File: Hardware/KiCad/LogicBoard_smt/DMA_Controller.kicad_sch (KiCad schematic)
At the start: 49 parts, among them IC1 7408N, IC18 7432N, IC20 7430N, IC21 7400N, IC3 74573N, IC31 7400N, IC32 7432N, IC5 7400N, IC53 7404N, IC9 7474N, U3 GFXL, U4 GFXH, U5 GFYL, U6 GFYH, U7 74LVC2G07

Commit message: updates to kicad smt versions
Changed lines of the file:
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@@
     (stroke (width 0.1524) (type solid))
   )
-  (wire (pts (xy 515.62 901.7) (xy 515.62 891.54))
+  (wire (pts (xy 515.62 901.7) (xy 515.62 892.81))
     (stroke (width 0.1524) (type solid))
   )
@@
     (stroke (width 0) (type default))
   )
-  (wire (pts (xy 520.7 901.7) (xy 515.62 901.7))
+  (wire (pts (xy 515.62 901.7) (xy 520.7 901.7))
     (stroke (width 0.1524) (type solid))
   )
@@
     (stroke (width 0.1524) (type solid))
   )
-  (wire (pts (xy 515.62 891.54) (xy 546.1 891.54))
+  (wire (pts (xy 515.62 892.81) (xy 546.1 892.81))
     (stroke (width 0.1524) (type solid))
   )
@@
     (stroke (width 0.1524) (type solid))
   )
-  (wire (pts (xy 513.08 741.68) (xy 513.08 474.98))
+  (wire (pts (xy 513.08 474.98) (xy 513.08 741.68))
     (stroke (width 0.1524) (type solid))
   )
@@
     (stroke (width 0) (type default))
   )
-  (wire (pts (xy 546.1 891.54) (xy 546.1 868.68))
+  (wire (pts (xy 546.1 892.81) (xy 546.1 868.68))
     (stroke (width 0.1524) (type solid))
   )
@@
     (stroke (width 0.1524) (type solid))
   )
+  (wire (pts (xy 513.08 711.2) (xy 513.08 708.66))
+    (stroke (width 0) (type default))
+  )
   (wire (pts (xy 462.28 1122.68) (xy 464.82 1122.68))
     (stroke (width 0.1524) (type solid))
@@
     (effects (font (size 1.27 1.27)) (justify left bottom))
   )
-  (label "~{INIT}" (at 513.08 708.66 90) (fields_autoplaced)
+  (label "~{INIT}" (at 513.08 711.2 90) (fields_autoplaced)
     (effects (font (size 1.2446 1.2446)) (justify left bottom))
   )
@@
     (effects (font (size 1.2446 1.2446)) (justify left bottom))
   )
+  (label "~{ROWCOMPLETE}" (at 524.51 892.81 0) (fields_autoplaced)
+    (effects (font (size 1.27 1.27)) (justify left bottom))
+  )
   (label "~{DIRECT-SELECT}" (at 506.73 269.24 90) (fields_autoplaced)
     (effects (font (size 1.2446 1.2446)) (justify left bottom))
@@
     (effects (font (size 1.2446 1.2446)) (justify left bottom))
   )
-  (label "~{ROWCOMPLETE}" (at 515.62 891.54 90) (fields_autoplaced)
-    (effects (font (size 1.2446 1.2446)) (justify left bottom))
-  )
   (label "VID_OUT_PAGE" (at 891.54 477.52 270) (fields_autoplaced)
     (effects (font (size 1.2446 1.2446)) (justify right bottom))
@@
     (effects (font (size 1.2446 1.2446)) (justify left bottom))
   )
-  (label "VNMI" (at 909.32 500.38 90) (fields_autoplaced)
-    (effects (font (size 1.2446 1.2446)) (justify left bottom))
-  )
   (label "IRQ-ENABLE" (at 459.74 170.18 0) (fields_autoplaced)
     (effects (font (size 1.2446 1.2446)) (justify left bottom))
@@
     )
   )
+  (global_label "VNMI" (shape input) (at 909.32 485.14 0) (fields_autoplaced)
+    (effects (font (size 1.27 1.27)) (justify left))
+    (property "Intersheetrefs" "${INTERSHEET_REFS}" (at 916.7805 485.14 0)
+      (effects (font (size 1.27 1.27)) (justify left) hide)
+    )
+  )
   (global_label "A3" (shape bidirectional) (at 388.62 27.94 0) (fields_autoplaced)
     (effects (font (size 1.3513 1.3513)) (justify left))
@@
       (effects (font (size 1.27 1.27)) hide)
     )
-    (property "Value" "VCC" (at 566.42 703.58 90)
+    (property "Value" "VCC" (at 563.88 699.77 90)
       (effects (font (size 1.778 1.5113)) (justify left bottom))
     )

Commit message: collect production documents for quoting
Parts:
- TO_FRAMEBUFFER1: footprint Connector_FFC-FPC:TE_4-1734839-0_1x40-1MP_P0.5mm_Horizontal -> SamacSys_Parts:F34G1A7Q1E8C40; MPN 4-1734839-0 -> F34G-1A7Q1-E8C40

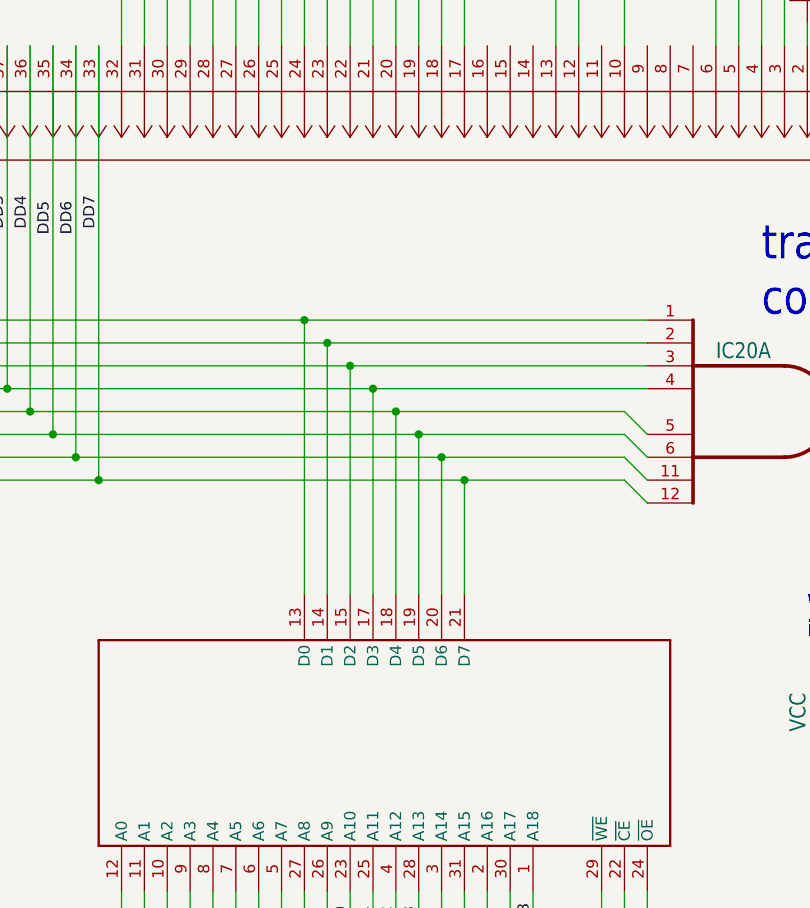
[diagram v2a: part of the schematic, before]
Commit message: replace dual ported frame buffer with mirrored single ported rams
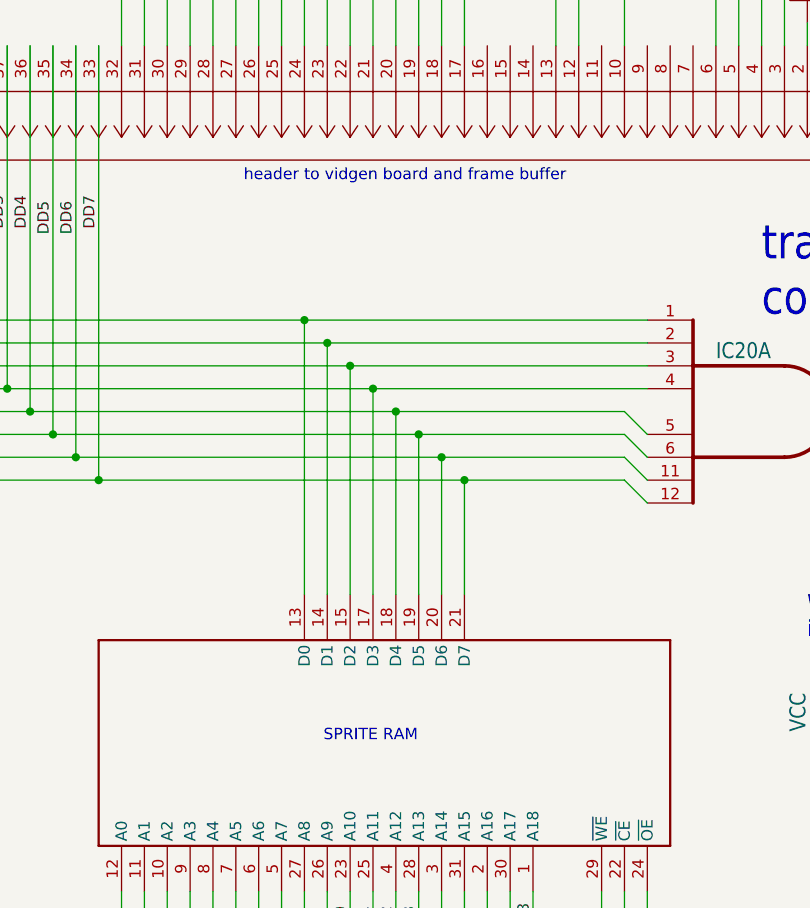
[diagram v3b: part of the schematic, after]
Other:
- note added: "SPRITE RAM"
- note added: "header to vidgen board and frame buffer"
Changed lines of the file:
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@@
+		)
+	)
+	(text "header to vidgen board and frame buffer"
+		(exclude_from_sim no)
+		(at 884.936 527.558 0)
+		(effects
+			(font
+				(size 1.27 1.27)
+			)
 		)
 	)
@@
 		)
 	)
+	(text "SPRITE RAM"
+		(exclude_from_sim no)
+		(at 881.126 589.788 0)
+		(effects
+			(font
+				(size 1.27 1.27)
+			)
+		)
+	)
